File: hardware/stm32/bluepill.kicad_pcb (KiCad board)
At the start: 2 copper layers, 50 x 100 mm, 82 parts, among them J1 LCD, J10 S3, J11 S4, J12 S5, J13 S6, J14 RTC, J15 +5V, J16 Conn_01x02_Male, J17 ESP-01, J18 USART1, J19 Buttons, J2 SD Card, J3 Radio, J4 Outer, J5 Inner, J6 LED Power, J7 Open, J8 S1, J9 S2, Q1 IRLML2502, Q2 IRLML2502, Q3 IRLML2502, Q4 IRLML2502, Q5 IRLML2502, Q6 IRLML2502, U1 PC817, U10 PC817, U11 PC817, U12 LM1117-3.3, U2 24LC512, U3 bluepill, U4 PC817, U5 PC817, U6 PC817, U7 PC817, U8 PC817, U9 PC817

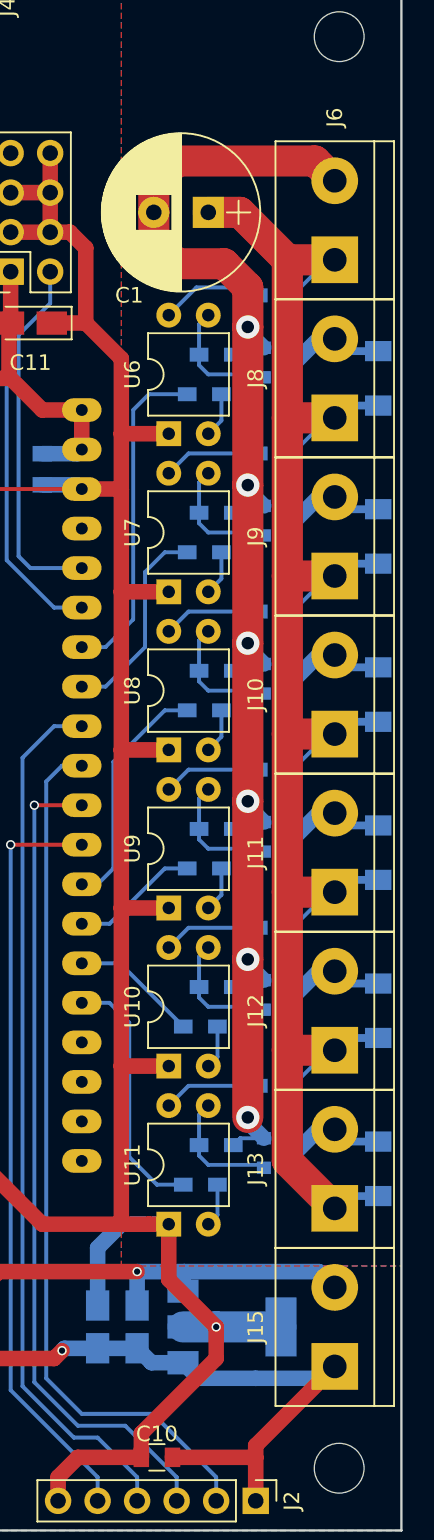
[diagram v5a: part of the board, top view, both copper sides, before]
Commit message: bluepill-hardware: few modifications on PCB after receiving the first proto panel
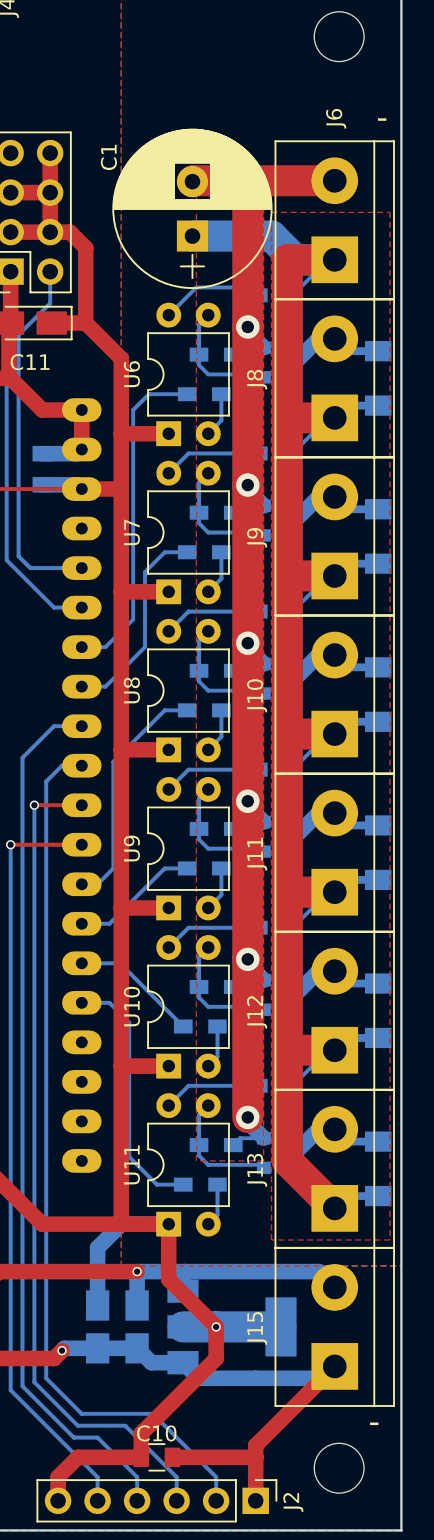
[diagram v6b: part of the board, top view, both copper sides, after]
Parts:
- moved C1 1.83 mm to (131.6, 51.8), turned to 90 degrees
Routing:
- net GNDPWR: track 101.3 -> 93.6 mm
- net +12V: track 127.5 -> 131.0 mm
- added copper zone on F.Cu, net +12V
- added copper zone on F.Cu, net GNDPWR
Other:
- board text added: "-"
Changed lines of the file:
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@@
     (area 79.435716 29.3 157.85 140.350001)
     (thickness 1.6)
-    (drawings 16)
-    (tracks 493)
+    (drawings 18)
+    (tracks 489)
     (zones 0)
     (modules 82)
@@
     (trace_clearance 0.2032)
     (zone_clearance 0.508)
-    (zone_45_only no)
+    (zone_45_only yes)
     (trace_min 0.2)
     (segment_width 0.2)
@@
   )
   (module Capacitors_THT:CP_Radial_D10.0mm_P3.50mm (layer F.Cu)
-    (at 132.588 50.292 180)
+    (at 131.572 51.816 90)
     (descr "CP, Radial series, Radial, pin pitch=3.50mm, , diameter=10mm, Electrolytic Capacitor")
     (tags "CP Radial series Radial pin pitch 3.50mm  diameter 10mm Electrolytic Capacitor")
-    (fp_text reference C1 (at 5.08 -5.334 180) (layer F.SilkS)
+    (fp_text reference C1 (at 5.08 -5.334 90) (layer F.SilkS)
       (effects (font (size 1 1) (thickness 0.15)))
     )
-    (fp_text value 220u (at 1.75 6.31 180) (layer F.Fab)
+    (fp_text value 220u (at 1.75 6.31 90) (layer F.Fab)
       (effects (font (size 1 1) (thickness 0.15)))
     )
@@
     (fp_line (start 7.1 5.35) (end 7.1 -5.35) (layer F.CrtYd) (width 0.05))
     (fp_line (start 7.1 -5.35) (end -3.6 -5.35) (layer F.CrtYd) (width 0.05))
-    (fp_text user %R (at 1.75 0 180) (layer F.Fab)
+    (fp_text user %R (at 1.75 0 90) (layer F.Fab)
       (effects (font (size 1 1) (thickness 0.15)))
     )
-    (pad 1 thru_hole rect (at 0 0 180) (size 2 2) (drill 1) (layers *.Cu *.Mask)
+    (pad 1 thru_hole rect (at 0 0 90) (size 2 2) (drill 1) (layers *.Cu *.Mask)
       (net 19 +12V))
-    (pad 2 thru_hole circle (at 3.5 0 180) (size 2 2) (drill 1) (layers *.Cu *.Mask)
+    (pad 2 thru_hole circle (at 3.5 0 90) (size 2 2) (drill 1) (layers *.Cu *.Mask)
       (net 42 GNDPWR))
     (model ${KISYS3DMOD}/Capacitors_THT.3dshapes/CP_Radial_D10.0mm_P3.50mm.wrl
@@
     )
   )
+  (gr_text "-\n" (at 143.256 128.016) (layer F.SilkS)
+    (effects (font (size 1.5 1.5) (thickness 0.3)))
+  )
+  (gr_text "-\n" (at 143.764 44.196) (layer F.SilkS)
+    (effects (font (size 1.5 1.5) (thickness 0.3)))
+  )
   (dimension 100 (width 0.3) (layer Dwgs.User)
     (gr_text "100,000 mm" (at 86.65 85 90) (layer Dwgs.User)
@@
   (segment (start 128.016 123.295) (end 128.941 124.22) (width 1) (layer B.Cu) (net 4))
   (segment (start 128.941 124.22) (end 130.962 124.22) (width 1) (layer B.Cu) (net 4))
-  (segment (start 130.048 115.316) (end 130.048 118.872) (width 1) (layer F.Cu) (net 5) (status 400000))
+  (segment (start 130.048 115.316) (end 130.048 118.872) (width 1) (layer F.Cu) (net 5))
   (segment (start 130.048 118.872) (end 133.096 121.92) (width 1) (layer F.Cu) (net 5))
   (segment (start 114.384 83.312) (end 114.384 70.02) (width 0.25) (layer B.Cu) (net 5))
@@
   (segment (start 112.014 66.802) (end 112.014 54.864) (width 0.254) (layer B.Cu) (net 18))
   (segment (start 110.744 68.072) (end 112.014 66.802) (width 0.254) (layer B.Cu) (net 18))
+  (segment (start 140.716 53.34) (end 138.176 53.34) (width 2) (layer B.Cu) (net 19) (status 400000))
+  (segment (start 136.652 51.816) (end 131.572 51.816) (width 2) (layer B.Cu) (net 19) (status 800000))
+  (segment (start 138.176 53.34) (end 136.652 51.816) (width 2) (layer B.Cu) (net 19))
   (segment (start 140.716 104.14) (end 137.668 104.14) (width 2) (layer F.Cu) (net 19))
   (segment (start 140.716 93.98) (end 137.668 93.98) (width 2) (layer F.Cu) (net 19))
@@
   (segment (start 140.716 73.66) (end 137.668 73.66) (width 2) (layer F.Cu) (net 19))
   (segment (start 140.716 63.5) (end 137.668 63.5) (width 2) (layer F.Cu) (net 19))
-  (segment (start 137.668 53.34) (end 134.62 50.292) (width 2) (layer F.Cu) (net 19))
-  (segment (start 134.62 50.292) (end 132.588 50.292) (width 2) (layer F.Cu) (net 19))
   (segment (start 137.668 111.252) (end 137.668 104.14) (width 2) (layer F.Cu) (net 19))
   (segment (start 140.716 114.3) (end 137.668 111.252) (width 2) (layer F.Cu) (net 19))
@@
   (segment (start 131.996 60.114) (end 132.588 60.706) (width 0.25) (layer B.Cu) (net 41))
   (segment (start 135.972 60.706) (end 136.16 60.894) (width 0.25) (layer B.Cu) (net 41))
-  (segment (start 129.088 50.292) (end 129.088 48.458) (width 2) (layer F.Cu) (net 42))
-  (segment (start 139.446 46.99) (end 140.716 48.26) (width 2) (layer F.Cu) (net 42))
-  (segment (start 130.556 46.99) (end 139.446 46.99) (width 2) (layer F.Cu) (net 42))
-  (segment (start 129.088 48.458) (end 130.556 46.99) (width 2) (layer F.Cu) (net 42))
-  (segment (start 135.128 57.658) (end 135.128 55.118) (width 2) (layer F.Cu) (net 42))
-  (segment (start 129.088 52.126) (end 129.088 50.292) (width 2) (layer F.Cu) (net 42))
-  (segment (start 130.556 53.594) (end 129.088 52.126) (width 2) (layer F.Cu) (net 42))
-  (segment (start 133.604 53.594) (end 130.556 53.594) (width 2) (layer F.Cu) (net 42))
-  (segment (start 135.128 55.118) (end 133.604 53.594) (width 2) (layer F.Cu) (net 42))
+  (segment (start 135.128 57.658) (end 135.128 48.26) (width 2) (layer F.Cu) (net 42))
+  (segment (start 140.716 48.26) (end 135.128 48.26) (width 2) (layer F.Cu) (net 42) (status 400000))
+  (segment (start 135.128 48.26) (end 131.628 48.26) (width 2) (layer F.Cu) (net 42) (status 800000))
+  (segment (start 131.628 48.26) (end 131.572 48.316) (width 2) (layer F.Cu) (net 42) (status C00000))
   (segment (start 136.16 109.794) (end 135.128 108.762) (width 1) (layer B.Cu) (net 42))
   (segment (start 135.128 108.458) (end 135.128 98.298) (width 2) (layer F.Cu) (net 42))
@@
       )
     )
+  )
+  (zone (net 19) (net_name +12V) (layer F.Cu) (hatch edge 0.508)
+    (connect_pads (clearance 0.508))
+    (min_thickness 0.254)
+    (fill yes (arc_segments 16) (thermal_gap 0.508) (thermal_bridge_width 0.508))
+    (polygon
+      (pts
+        (xy 136.652 50.292) (xy 144.272 50.292) (xy 144.272 116.332) (xy 136.652 116.332)
+      )
+    )
+  )
+  (zone (net 42) (net_name GNDPWR) (layer F.Cu) (hatch edge 0.508)
+    (connect_pads (clearance 0.508))
+    (min_thickness 0.254)
+    (fill yes (arc_segments 16) (thermal_gap 0.508) (thermal_bridge_width 0.508))
+    (polygon
+      (pts
+        (xy 131.826 48.768) (xy 136.144 48.768) (xy 136.144 54.356) (xy 136.144 111.252) (xy 131.826 111.252)
+      )
+    )
